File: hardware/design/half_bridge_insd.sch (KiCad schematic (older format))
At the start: 17 parts

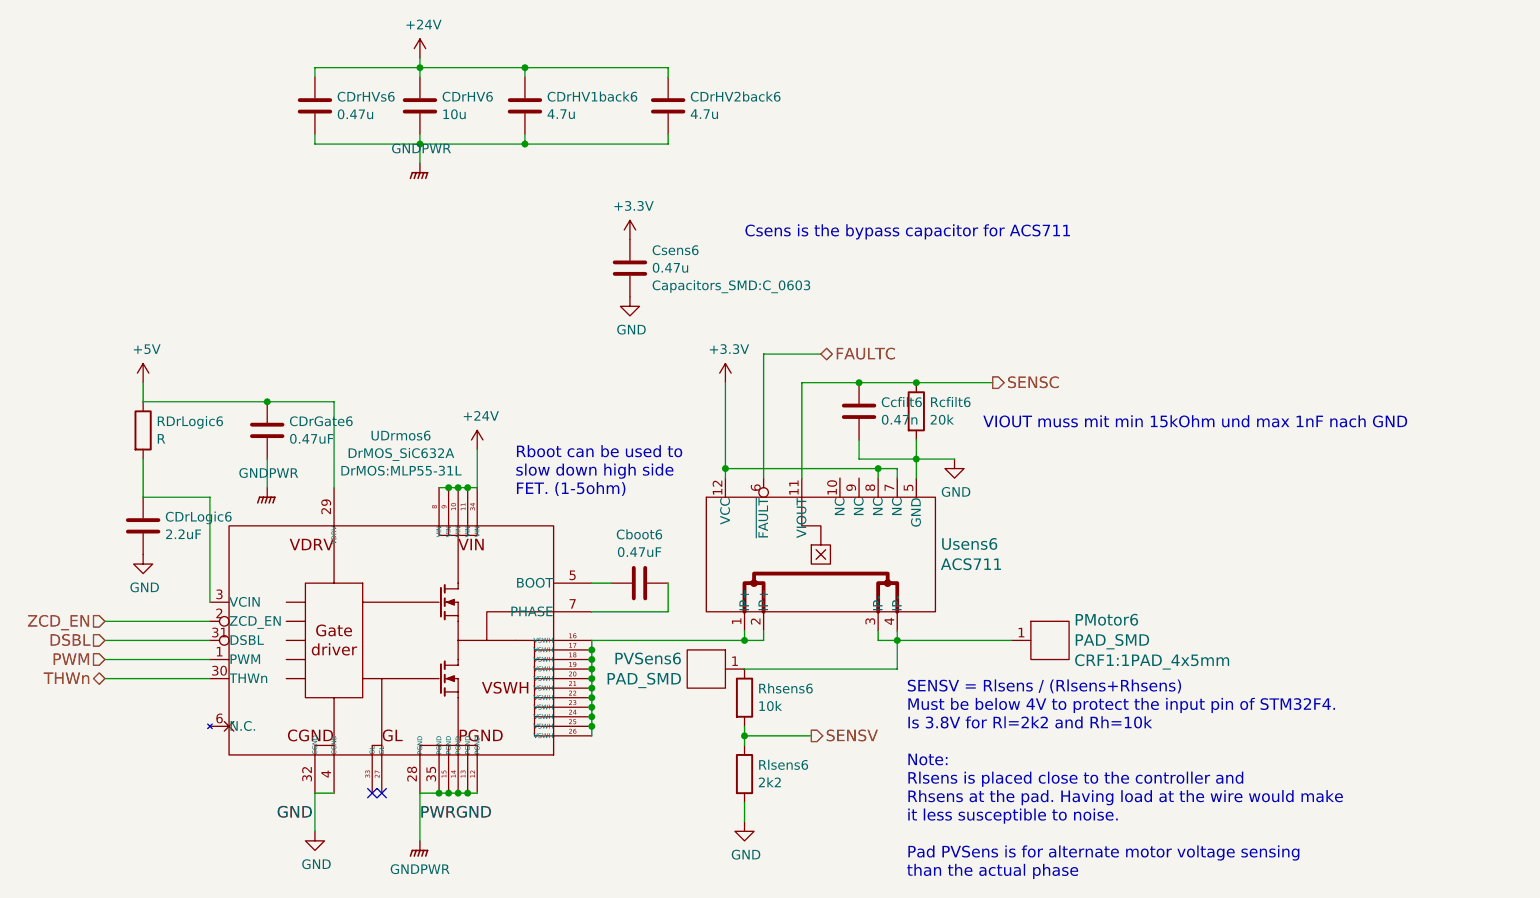
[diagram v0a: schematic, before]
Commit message: TODO Double-check BOM. Check silk screen. Check Gerber output.
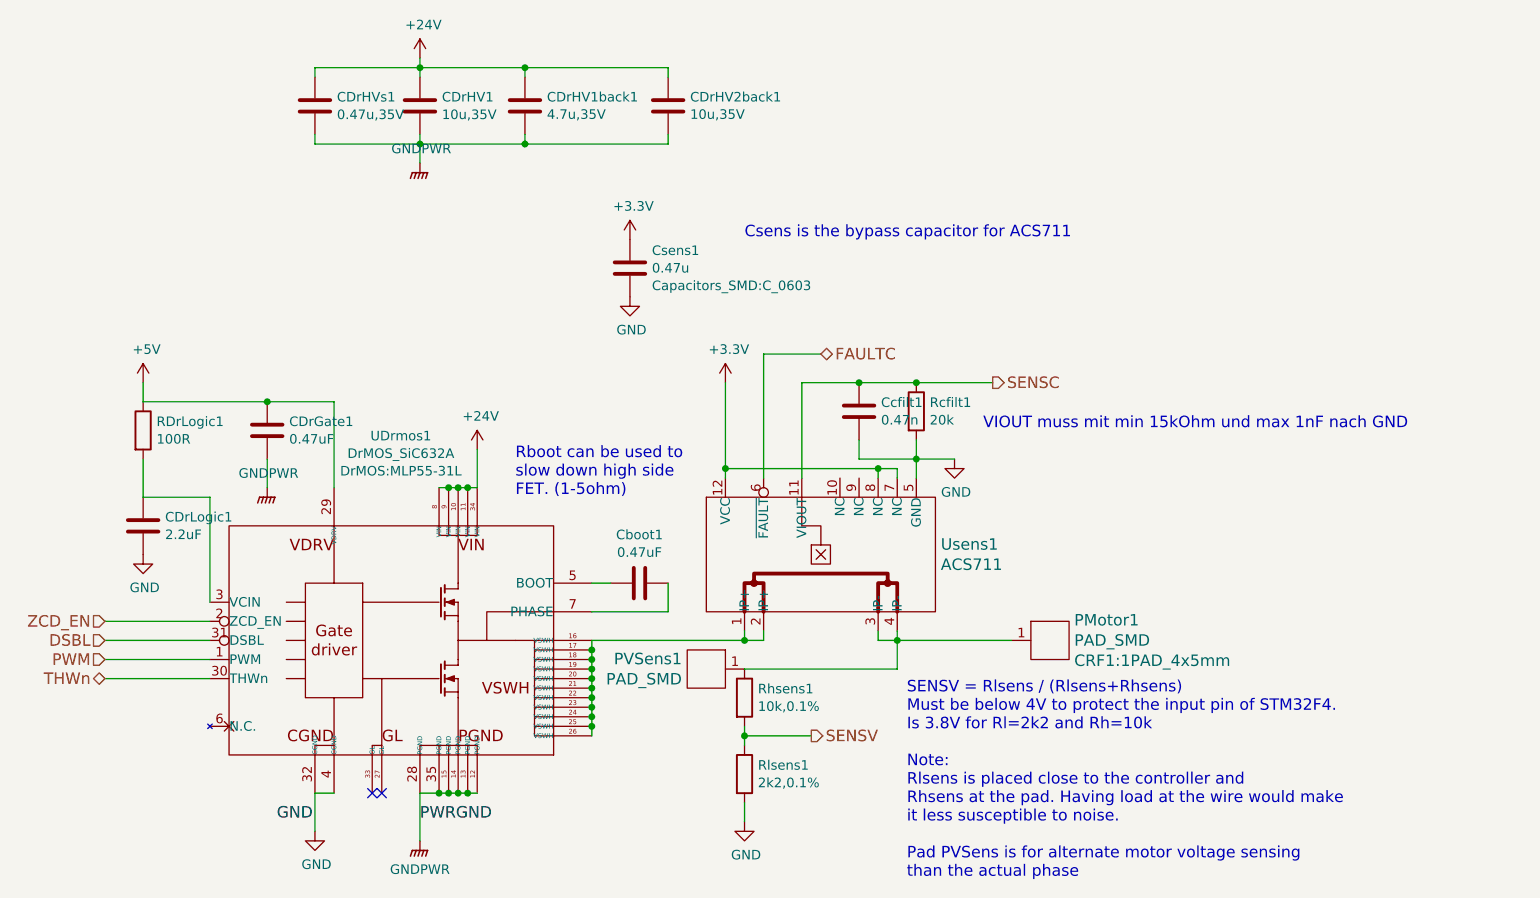
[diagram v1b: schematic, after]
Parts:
- CDrHV1: value 10u -> 10u,35V; Comment (none) -> dc link, X7R, >35V
- CDrHV1back1: value 4.7u -> 4.7u,35V; Comment (none) -> dc link, X7R, >35V
- CDrHV2back1: value 4.7u -> 10u,35V; Comment (none) -> dc link, X5R, >35V
- CDrHVs1: value 0.47u -> 0.47u,35V; Comment (none) -> dc link, X7R, >35V
- Csens1: Comment X7R, >10V -> bypass capacitor for ACS711, X7R, >10V
- RDrLogic1: value R -> 100R
- Rhsens1: value 10k -> 10k,0.1%
- Rlsens1: value 2k2 -> 2k2,0.1%
- UDrmos1: Part Number SiC632CD-T1-GE3 -> SiC632ACD-T1-GE3
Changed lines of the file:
@@
 AR Path="/56BA2E2B/55DF8D4F" Ref="Cboot5"  Part="1"
 AR Path="/56BA5F82/55DF8D4F" Ref="Cboot6"  Part="1"
-F 0 "Cboot6" V 6647 3700 50  0000 C CNN
+F 0 "Cboot1" V 6647 3700 50  0000 C CNN
 F 1 "0.47uF" V 6739 3700 50  0000 C CNN
 F 2 "Capacitors_SMD:C_0603_HandSoldering" H 6938 3550 30  0001 C CNN
@@
 AR Path="/56BA2E2B/55DF8D84" Ref="CDrGate5"  Part="1"
 AR Path="/56BA5F82/55DF8D84" Ref="CDrGate6"  Part="1"
-F 0 "CDrGate6" H 5065 2946 50  0000 L CNN
+F 0 "CDrGate1" H 5065 2946 50  0000 L CNN
 F 1 "0.47uF" H 5065 2854 50  0000 L CNN
 F 2 "Capacitors_SMD:C_0603_HandSoldering" H 4988 2750 30  0001 C CNN
@@
 AR Path="/56BA2E2B/56984538" Ref="Usens5"  Part="1"
 AR Path="/56BA5F82/56984538" Ref="Usens6"  Part="1"
-F 0 "Usens6" V 7797 2922 60  0000 R CNN
+F 0 "Usens1" V 7797 2922 60  0000 R CNN
 F 1 "ACS711" V 7903 2922 60  0000 R CNN
 F 2 "Allegro:QFN-12-1EX_3x3mm_Pitch0.5mm" V 7956 2922 60  0001 R CNN
@@
 AR Path="/56BA2E2B/56A19C85" Ref="UDrmos5"  Part="1"
 AR Path="/56BA5F82/56A19C85" Ref="UDrmos6"  Part="1"
-F 0 "UDrmos6" H 5650 5071 50  0000 C CNN
+F 0 "UDrmos1" H 5650 5071 50  0000 C CNN
 F 1 "DrMOS_SiC632A" H 5650 4979 50  0000 C CNN
 F 2 "DrMOS:MLP55-31L" H 5650 4887 50  0000 C CNN
 F 3 "" H 5850 3800 50  0000 C CNN
 F 4 "Vishay" H 5850 4000 60  0001 C CNN "Manufacturer"
-F 5 "SiC632CD-T1-GE3" H 5850 4000 60  0001 C CNN "Part Number"
+F 5 "SiC632ACD-T1-GE3" H 5850 4000 60  0001 C CNN "Part Number"
 	1    5850 4000
 	1    0    0    -1
@@
 AR Path="/56BA2E2B/56A2AE4F" Ref="#PWR078"  Part="1"
 AR Path="/56BA5F82/56A2AE4F" Ref="#PWR091"  Part="1"
-F 0 "#PWR091" H 5750 4850 50  0001 C CNN
+F 0 "#PWR014" H 5750 4850 50  0001 C CNN
 F 1 "GNDPWR" H 5750 4900 50  0000 C CNN
 F 2 "" H 5750 5000 50  0000 C CNN
@@
 AR Path="/56BA2E2B/56A2B769" Ref="#PWR079"  Part="1"
 AR Path="/56BA5F82/56A2B769" Ref="#PWR092"  Part="1"
-F 0 "#PWR092" H 5200 4750 50  0001 C CNN
+F 0 "#PWR015" H 5200 4750 50  0001 C CNN
 F 1 "GND" H 5208 4826 50  0000 C CNN
 F 2 "" H 5200 5000 50  0000 C CNN
@@
 AR Path="/56BA2E2B/56A2BBEE" Ref="#PWR080"  Part="1"
 AR Path="/56BA5F82/56A2BBEE" Ref="#PWR093"  Part="1"
-F 0 "#PWR093" H 4950 3000 50  0001 C CNN
+F 0 "#PWR016" H 4950 3000 50  0001 C CNN
 F 1 "GNDPWR" H 4957 3275 50  0000 C CNN
 F 2 "" H 4950 3150 50  0000 C CNN
@@
 AR Path="/56BA2E2B/56A2CDC4" Ref="CDrLogic5"  Part="1"
 AR Path="/56BA5F82/56A2CDC4" Ref="CDrLogic6"  Part="1"
-F 0 "CDrLogic6" H 4415 3446 50  0000 L CNN
+F 0 "CDrLogic1" H 4415 3446 50  0000 L CNN
 F 1 "2.2uF" H 4415 3354 50  0000 L CNN
 F 2 "Capacitors_SMD:C_0603" H 4338 3250 30  0001 C CNN
@@
 AR Path="/56BA2E2B/56A2CDEC" Ref="#PWR081"  Part="1"
 AR Path="/56BA5F82/56A2CDEC" Ref="#PWR094"  Part="1"
-F 0 "#PWR094" H 4300 3300 50  0001 C CNN
+F 0 "#PWR017" H 4300 3300 50  0001 C CNN
 F 1 "GND" H 4308 3376 50  0000 C CNN
 F 2 "" H 4300 3550 50  0000 C CNN
@@
 AR Path="/56BA2E2B/56A2CF9B" Ref="#PWR082"  Part="1"
 AR Path="/56BA5F82/56A2CF9B" Ref="#PWR095"  Part="1"
-F 0 "#PWR095" H 4300 2500 50  0001 C CNN
+F 0 "#PWR018" H 4300 2500 50  0001 C CNN
 F 1 "+5V" H 4318 2824 50  0000 C CNN
 F 2 "" H 4300 2650 50  0000 C CNN
@@
 AR Path="/56BA2E2B/56A2D0BC" Ref="RDrLogic5"  Part="1"
 AR Path="/56BA5F82/56A2D0BC" Ref="RDrLogic6"  Part="1"
-F 0 "RDrLogic6" H 4370 2946 50  0000 L CNN
-F 1 "R" H 4370 2854 50  0000 L CNN
+F 0 "RDrLogic1" H 4370 2946 50  0000 L CNN
+F 1 "100R" H 4370 2854 50  0000 L CNN
 F 2 "Resistors_SMD:R_0603" V 4230 2900 50  0001 C CNN
 F 3 "" H 4300 2900 50  0000 C CNN
@@
 AR Path="/56BA2E2B/56A2EFF6" Ref="#PWR083"  Part="1"
 AR Path="/56BA5F82/56A2EFF6" Ref="#PWR096"  Part="1"
-F 0 "#PWR096" H 8550 2800 50  0001 C CNN
+F 0 "#PWR019" H 8550 2800 50  0001 C CNN
 F 1 "GND" H 8558 2876 50  0000 C CNN
 F 2 "" H 8550 3050 50  0000 C CNN
@@
 AR Path="/56BA2E2B/56A2FD69" Ref="Rhsens5"  Part="1"
 AR Path="/56BA5F82/56A2FD69" Ref="Rhsens6"  Part="1"
-F 0 "Rhsens6" H 7520 4346 50  0000 L CNN
-F 1 "10k" H 7520 4254 50  0000 L CNN
+F 0 "Rhsens1" H 7520 4346 50  0000 L CNN
+F 1 "10k,0.1%" H 7520 4254 50  0000 L CNN
 F 2 "Capacitors_SMD:C_0603_HandSoldering" V 7380 4300 50  0001 C CNN
 F 3 "" H 7450 4300 50  0000 C CNN
@@
 AR Path="/56BA2E2B/56A2FEAC" Ref="Rlsens5"  Part="1"
 AR Path="/56BA5F82/56A2FEAC" Ref="Rlsens6"  Part="1"
-F 0 "Rlsens6" H 7520 4746 50  0000 L CNN
-F 1 "2k2" H 7520 4654 50  0000 L CNN
+F 0 "Rlsens1" H 7520 4746 50  0000 L CNN
+F 1 "2k2,0.1%" H 7520 4654 50  0000 L CNN
 F 2 "Resistors_SMD:R_0402" V 7380 4700 50  0001 C CNN
 F 3 "" H 7450 4700 50  0000 C CNN
@@
 AR Path="/56BA2E2B/56A30067" Ref="#PWR084"  Part="1"
 AR Path="/56BA5F82/56A30067" Ref="#PWR097"  Part="1"
-F 0 "#PWR097" H 7450 4700 50  0001 C CNN
+F 0 "#PWR020" H 7450 4700 50  0001 C CNN
 F 1 "GND" H 7458 4776 50  0000 C CNN
 F 2 "" H 7450 4950 50  0000 C CNN
@@
 AR Path="/56BA2E2B/56A31D68" Ref="#PWR085"  Part="1"
 AR Path="/56BA5F82/56A31D68" Ref="#PWR098"  Part="1"
-F 0 "#PWR098" H 6050 2850 50  0001 C CNN
+F 0 "#PWR021" H 6050 2850 50  0001 C CNN
 F 1 "+24V" H 6068 3174 50  0000 C CNN
 F 2 "" H 6050 3000 50  0000 C CNN
@@
 AR Path="/56BA2E2B/56A32138" Ref="#PWR086"  Part="1"
 AR Path="/56BA5F82/56A32138" Ref="#PWR099"  Part="1"
-F 0 "#PWR099" H 7350 2500 50  0001 C CNN
+F 0 "#PWR022" H 7350 2500 50  0001 C CNN
 F 1 "+3.3V" H 7368 2824 50  0000 C CNN
 F 2 "" H 7350 2650 50  0000 C CNN
@@
 AR Path="/56BA2E2B/56A3225A" Ref="Rcfilt5"  Part="1"
 AR Path="/56BA5F82/56A3225A" Ref="Rcfilt6"  Part="1"
-F 0 "Rcfilt6" H 8420 2846 50  0000 L CNN
+F 0 "Rcfilt1" H 8420 2846 50  0000 L CNN
 F 1 "20k" H 8420 2754 50  0000 L CNN
 F 2 "Resistors_SMD:R_0402" V 8280 2800 50  0001 C CNN
@@
 AR Path="/56BA2E2B/56A3233B" Ref="Ccfilt5"  Part="1"
 AR Path="/56BA5F82/56A3233B" Ref="Ccfilt6"  Part="1"
-F 0 "Ccfilt6" H 8165 2846 50  0000 L CNN
+F 0 "Ccfilt1" H 8165 2846 50  0000 L CNN
 F 1 "0.47n" H 8165 2754 50  0000 L CNN
 F 2 "Capacitors_SMD:C_0402" H 8088 2650 50  0001 C CNN
@@
 AR Path="/56BA2E2B/56A69AD2" Ref="#PWR087"  Part="1"
 AR Path="/56BA5F82/56A69AD2" Ref="#PWR0100"  Part="1"
-F 0 "#PWR0100" H 5750 800 50  0001 C CNN
+F 0 "#PWR023" H 5750 800 50  0001 C CNN
 F 1 "+24V" H 5768 1124 50  0000 C CNN
 F 2 "" H 5750 950 50  0000 C CNN
@@
 AR Path="/56BA2E2B/56A69B0E" Ref="CDrHV5"  Part="1"
 AR Path="/56BA5F82/56A69B0E" Ref="CDrHV6"  Part="1"
-F 0 "CDrHV6" H 5865 1246 50  0000 L CNN
-F 1 "10u" H 5865 1154 50  0000 L CNN
+F 0 "CDrHV1" H 5865 1246 50  0000 L CNN
+F 1 "10u,35V" H 5865 1154 50  0000 L CNN
 F 2 "Capacitors_SMD:C_1206" H 5788 1050 50  0001 C CNN
 F 3 "" H 5750 1200 50  0000 C CNN
+F 4 "dc link, X7R, >35V" H 5750 1200 60  0001 C CNN "Comment"
 	1    5750 1200
 	1    0    0    -1
@@
 AR Path="/56BA2E2B/56A69BA7" Ref="#PWR088"  Part="1"
 AR Path="/56BA5F82/56A69BA7" Ref="#PWR0101"  Part="1"
-F 0 "#PWR0101" H 5750 1300 50  0001 C CNN
+F 0 "#PWR024" H 5750 1300 50  0001 C CNN
 F 1 "GNDPWR" H 5757 1575 50  0000 C CNN
 F 2 "" H 5750 1450 50  0000 C CNN
@@
 AR Path="/56BA2E2B/56AF6D20" Ref="CDrHVs5"  Part="1"
 AR Path="/56BA5F82/56AF6D20" Ref="CDrHVs6"  Part="1"
-F 0 "CDrHVs6" H 5315 1246 50  0000 L CNN
-F 1 "0.47u" H 5315 1154 50  0000 L CNN
+F 0 "CDrHVs1" H 5315 1246 50  0000 L CNN
+F 1 "0.47u,35V" H 5315 1154 50  0000 L CNN
 F 2 "Capacitors_SMD:C_0603" H 5315 1108 50  0001 L CNN
 F 3 "" H 5200 1200 50  0000 C CNN
+F 4 "dc link, X7R, >35V" H 5200 1200 60  0001 C CNN "Comment"
 	1    5200 1200
 	1    0    0    -1
@@
 AR Path="/56BA2E2B/56B30AD6" Ref="PMotor5"  Part="1"
 AR Path="/56BA5F82/56B30AD6" Ref="PMotor6"  Part="1"
-F 0 "PMotor6" H 9177 4106 60  0000 L CNN
+F 0 "PMotor1" H 9177 4106 60  0000 L CNN
 F 1 "PAD_SMD" H 9177 4000 60  0000 L CNN
 F 2 "CRF1:1PAD_4x5mm" H 9177 3894 60  0000 L CNN
@@
 AR Path="/56BA2E2B/56B897AB" Ref="Csens5"  Part="1"
 AR Path="/56BA5F82/56B897AB" Ref="Csens6"  Part="1"
-F 0 "Csens6" H 6965 2142 50  0000 L CNN
+F 0 "Csens1" H 6965 2142 50  0000 L CNN
 F 1 "0.47u" H 6965 2050 50  0000 L CNN
 F 2 "Capacitors_SMD:C_0603" H 6965 1958 50  0000 L CNN
 F 3 "" H 6850 2050 50  0000 C CNN
-F 4 "X7R, >10V" H 6850 2050 60  0001 C CNN "Comment"
+F 4 "bypass capacitor for ACS711, X7R, >10V" H 6850 2050 60  0001 C CNN "Comment"
 	1    6850 2050
 	1    0    0    -1
@@
 AR Path="/56BA2E2B/56B89931" Ref="#PWR089"  Part="1"
 AR Path="/56BA5F82/56B89931" Ref="#PWR0102"  Part="1"
-F 0 "#PWR0102" H 6850 1950 50  0001 C CNN
+F 0 "#PWR025" H 6850 1950 50  0001 C CNN
 F 1 "GND" H 6858 2026 50  0000 C CNN
 F 2 "" H 6850 2200 50  0000 C CNN
@@
 AR Path="/56BA2E2B/56B89961" Ref="#PWR090"  Part="1"
 AR Path="/56BA5F82/56B89961" Ref="#PWR0103"  Part="1"
-F 0 "#PWR0103" H 6850 1750 50  0001 C CNN
+F 0 "#PWR026" H 6850 1750 50  0001 C CNN
 F 1 "+3.3V" H 6868 2074 50  0000 C CNN
 F 2 "" H 6850 1900 50  0000 C CNN
@@
 AR Path="/56BA2E2B/578D654C" Ref="CDrHV1back5"  Part="1"
 AR Path="/56BA5F82/578D654C" Ref="CDrHV1back6"  Part="1"
-F 0 "CDrHV1back6" H 6415 1246 50  0000 L CNN
-F 1 "4.7u" H 6415 1155 50  0000 L CNN
+F 0 "CDrHV1back1" H 6415 1246 50  0000 L CNN
+F 1 "4.7u,35V" H 6415 1155 50  0000 L CNN
 F 2 "Capacitors_SMD:C_1206" H 6338 1050 50  0001 C CNN
 F 3 "" H 6300 1200 50  0000 C CNN
+F 4 "dc link, X7R, >35V" H 6300 1200 60  0001 C CNN "Comment"
 	1    6300 1200
 	1    0    0    -1
@@
 AR Path="/56BA2E2B/578D76CB" Ref="CDrHV2back5"  Part="1"
 AR Path="/56BA5F82/578D76CB" Ref="CDrHV2back6"  Part="1"
-F 0 "CDrHV2back6" H 7165 1246 50  0000 L CNN
-F 1 "4.7u" H 7165 1155 50  0000 L CNN
+F 0 "CDrHV2back1" H 7165 1246 50  0000 L CNN
+F 1 "10u,35V" H 7165 1155 50  0000 L CNN
 F 2 "Capacitors_SMD:C_1206_HandSoldering" H 7088 1050 50  0001 C CNN
 F 3 "" H 7050 1200 50  0000 C CNN
+F 4 "dc link, X5R, >35V" H 7050 1200 60  0001 C CNN "Comment"
 	1    7050 1200
 	1    0    0    -1
@@
 AR Path="/56BA2E2B/57981B05" Ref="PVSens5"  Part="1"
 AR Path="/56BA5F82/57981B05" Ref="PVSens6"  Part="1"
-F 0 "PVSens6" H 7378 4203 60  0000 L CNN
+F 0 "PVSens1" H 7378 4203 60  0000 L CNN
 F 1 "PAD_SMD" H 7378 4097 60  0000 L CNN
 F 2 "Pads:PAD_SMD_1x1" H 7250 3900 60  0001 C CNN

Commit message: Added just a few words...
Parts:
- Ccfilt1: Comment (none) -> Use COG or NPO ceramic. Or poly- propylene or carbonate
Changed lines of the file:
@@
 F 2 "Capacitors_SMD:C_0402" H 8088 2650 50  0001 C CNN
 F 3 "" H 8050 2800 50  0000 C CNN
+F 4 "Use COG or NPO ceramic. Or poly- propylene or carbonate" H 8050 2800 60  0001 C CNN "Comment"
 	1    8050 2800
 	1    0    0    -1
